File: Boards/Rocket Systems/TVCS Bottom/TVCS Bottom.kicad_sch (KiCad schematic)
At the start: 105 parts, among them J1 Conn_01x01_Socket, J10 Conn_01x01_Socket, J11 Conn_01x01_Socket, J12 Conn_01x01_Socket, J13 Conn_01x01_Socket, J14 Conn_01x01_Socket, J15 Conn_01x01_Socket, J2 Conn_01x01_Socket, J3 XT30UPB-M, J4 XT30UPB-M, J5 Conn_01x01_Socket, J6 XT30UPB-M, J8 Conn_01x01_Socket, J9 Conn_01x01_Socket, Q1 2N7002H6327XTSA2, U1 MAX31856MUD+T, U10 MAX31856MUD+T, U11 IRLZ44NPBF, U12 IRLZ44NPBF, U13 LM61460AASQRJRRQ1, U14 ADS1114IRUGR, U15 TPS1120DR, U16 TPS1120DR, U3 MAX31856MUD+T, U4 MAX485CSA+T, U5 MCP9808T-E/MC, U8 PCA9306DP_118, U9 LM61460AASQRJRRQ1

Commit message: Repo Refactor and new systems update
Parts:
- removed LED6, LED7, LED8, LED9: HSMH-H191, Red SMD LED:HSMHH191, symbol Red SMD LED:HSMH-H191
- removed U15, U16: TPS1120DR, 2 PMOS:D8, symbol Dual PMOS TPS1120DR:TPS1120DR
- removed U4: MAX485CSA+T, RS Transceiver:21-0041-3-M_90-0096-8L_MXM, symbol RS_Transceiver_MAX485:MAX485CSA+T
- removed U8: PCA9306DP_118, I2C Voltage Translator:TSSOP8_SOT505-1_NXP, symbol I2C Voltage Translator:PCA9306DP_118
- added CR2, CR3, CR4, CR5: VLMC3100-GS08, LED_PLCC_VSMB, symbol GreenLED__VLMC3100-GS08:VLMC3100-GS08
- added U15, U8: TPS1120DR, D8, symbol TPS1120DR:TPS1120DR
- added U17: MAX485CSA+T, 21-0041-3-M_90-0096-8L_MXM, symbol RS_Transceiver:MAX485CSA+T
- added U4: PCA9306DP_118, TSSOP8_SOT505-1_NXP, symbol NXP PCA9306DP:PCA9306DP_118
- D1, D3: footprint Schottky RSX301L:DIOM5026X220N -> DIOM5026X220N
- J3, J4, J6: footprint AMASS_XT30UPB-M:CONN_XT30UPB-M_AMA -> CONN_XT30UPB-M_AMA
- Q1: footprint (none) -> PG-SOT23-3-5_INF_MIN
- U1, U10, U3: footprint Thermocouple:21-0066J_14_MXM -> 21-0066J_14_MXM
- U11, U12: footprint NMOS IRLZ44:PG-TO220-3_INF -> PG-TO220-3_INF
- U13, U9: footprint DCDC_LM61460:VQFN-HR14_RJR_TEX -> VQFN-HR14_RJR_TEX
- U14: footprint ADS1114:RUG10 -> RUG10
- U5: footprint MCP9808-TempSensor:DFN8_2x3MC_MCH -> DFN8_2x3MC_MCH
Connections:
- net +3.3V: now also U4.2 (VREF1)
- net +5V: now also U17.8 (VCC)
- net ADC SDA I2C: now also U4.4 (SDA1)
- net ADC SDL I2C: now also U4.3 (SCL1)
- net GND: now also CR2.1, CR3.1, CR4.1, CR5.1, U17.5 (GND), U4.1 (GND)
- net RS_ENABLE: now also U15.4 (2GATE), U17.2 (*RE), U17.3 (DE)
- net RS_RX: now also U17.1 (RO)
- net RS_TX: now also U17.4 (DI)
- net THERMO1_~{CS}: now also U8.2 (1GATE)
- net THERMO2_~{CS}: now also U8.4 (2GATE)
- net THERMO3_~{CS}: now also U15.2 (1GATE)
- net at C23.1, R4.1: now also U4.7 (VREF2), U4.8 (EN)
- net at R18.1: now also U8.1 (1SOURCE)
- net at R19.1: now also U8.3 (2SOURCE)
- net at J2.1 (Pin_1), R15.1, R16.1: now also U17.7 (B)
- net at J5.1 (Pin_1), R11.2, R16.2: now also U17.6 (A)
- net at R34.2, U14.10 (SCL): now also U4.6 (SCL2)
- net at R40.2, U14.9 (SDA): now also U4.5 (SDA2)
- net at R20.1: now also U15.1 (1SOURCE)
- net at R21.1: now also U15.3 (2SOURCE)
- new net: CR3.2, U8.5 (2DRAIN), U8.6 (2DRAIN)
- new net: CR5.2, U15.5 (2DRAIN), U15.6 (2DRAIN)
- new net: CR4.2, U15.7 (1DRAIN), U15.8 (1DRAIN)
- new net: CR2.2, U8.7 (1DRAIN), U8.8 (1DRAIN)
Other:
- sheet RP2040 Standard ports: added GPIO10, GPIO9; removed GP10/SPI1 SCK, GP9/SPI1 ~{CS}
- title: CANha Board -> Temperature & Valve Control System B
- moved on the sheet: R18, R19, R20, R21

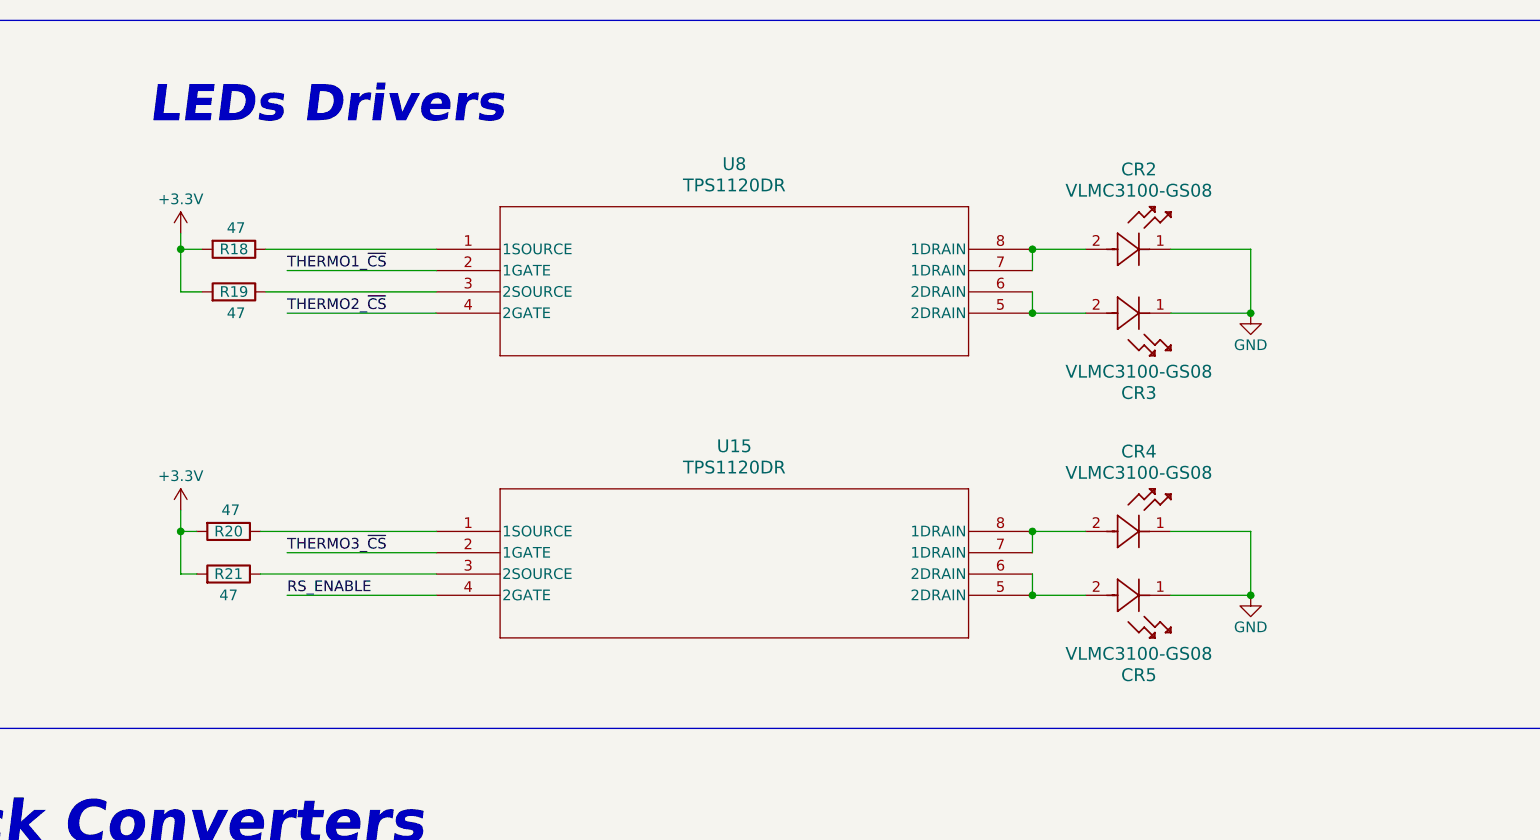
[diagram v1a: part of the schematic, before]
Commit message: Led driver circuit correction & RF FEM implementation
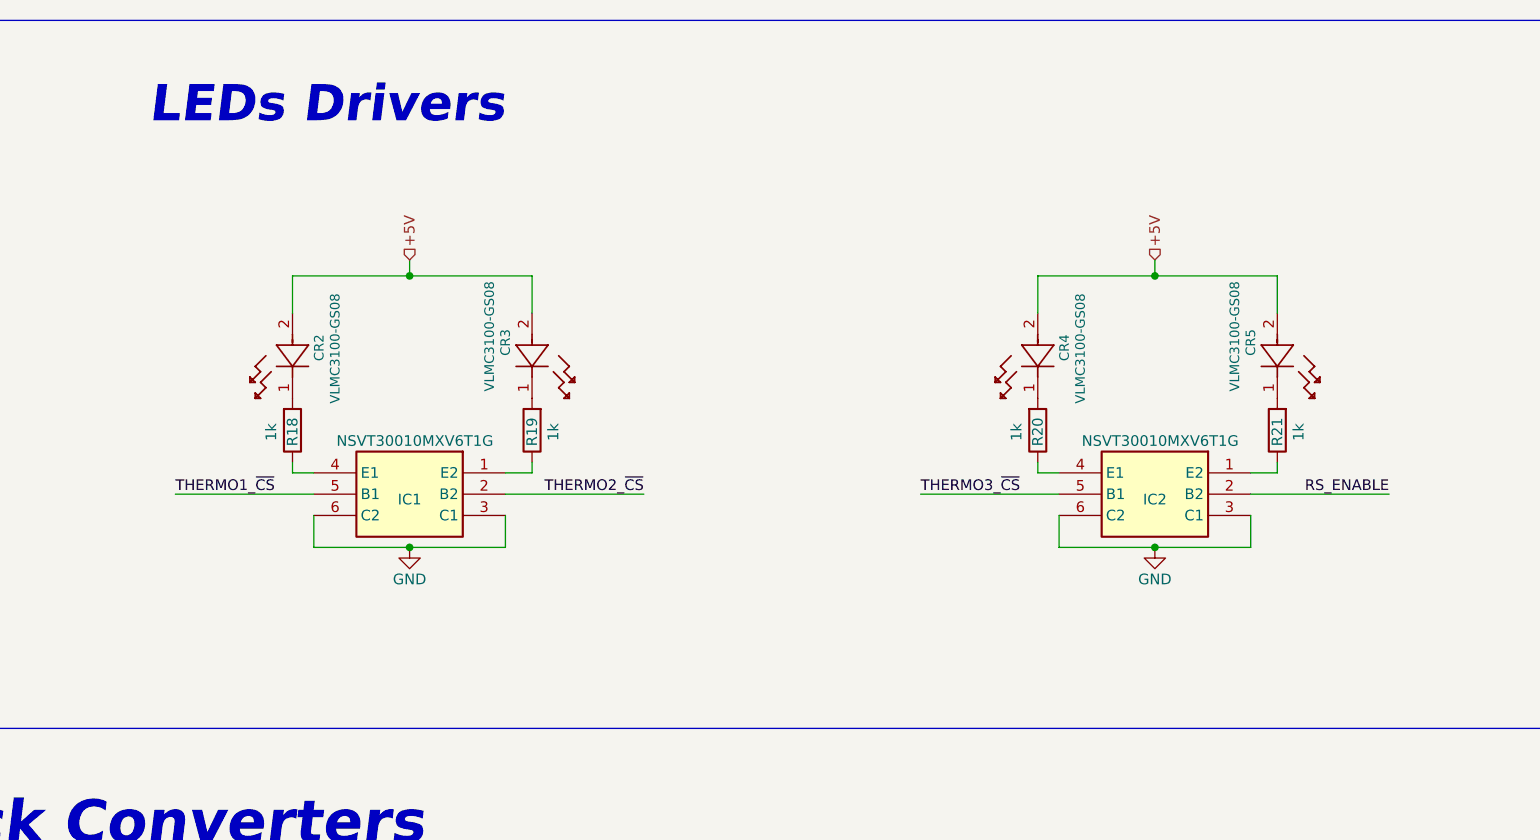
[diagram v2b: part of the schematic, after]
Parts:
- removed U15, U8: TPS1120DR, D8, symbol TPS1120DR:TPS1120DR
- added IC1, IC2: NSVT30010MXV6T1G, SOTFL50P160X60-6N, symbol NSVT30010MXV6T1G:NSVT30010MXV6T1G
- R18, R19, R20, R21: value 47 -> 1k; footprint RES_0402:RES_0402 -> RC0402N_VIS:RC0402N_VIS
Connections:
- net +3.3V: no longer R18.2, R19.2, R20.2, R21.2
- net +5V: now also CR2.2, CR3.2, CR4.2, CR5.2
- net GND: now also IC1.3 (C1), IC1.6 (C2), IC2.3 (C1), IC2.6 (C2); no longer CR2.1, CR3.1, CR4.1, CR5.1
- net RS_ENABLE: now also IC2.2 (B2)
- net THERMO1_~{CS}: now also IC1.5 (B1)
- net THERMO2_~{CS}: now also IC1.2 (B2)
- net THERMO3_~{CS}: now also IC2.5 (B1)
- net at R19.1: now also IC1.1 (E2)
- net at R21.1: now also IC2.1 (E2)
- net at R20.1: now also IC2.4 (E1)
- net at R18.1: now also IC1.4 (E1)
- new net: CR2.1, R18.2
- new net: CR5.1, R21.2
- new net: CR4.1, R20.2
- new net: CR3.1, R19.2

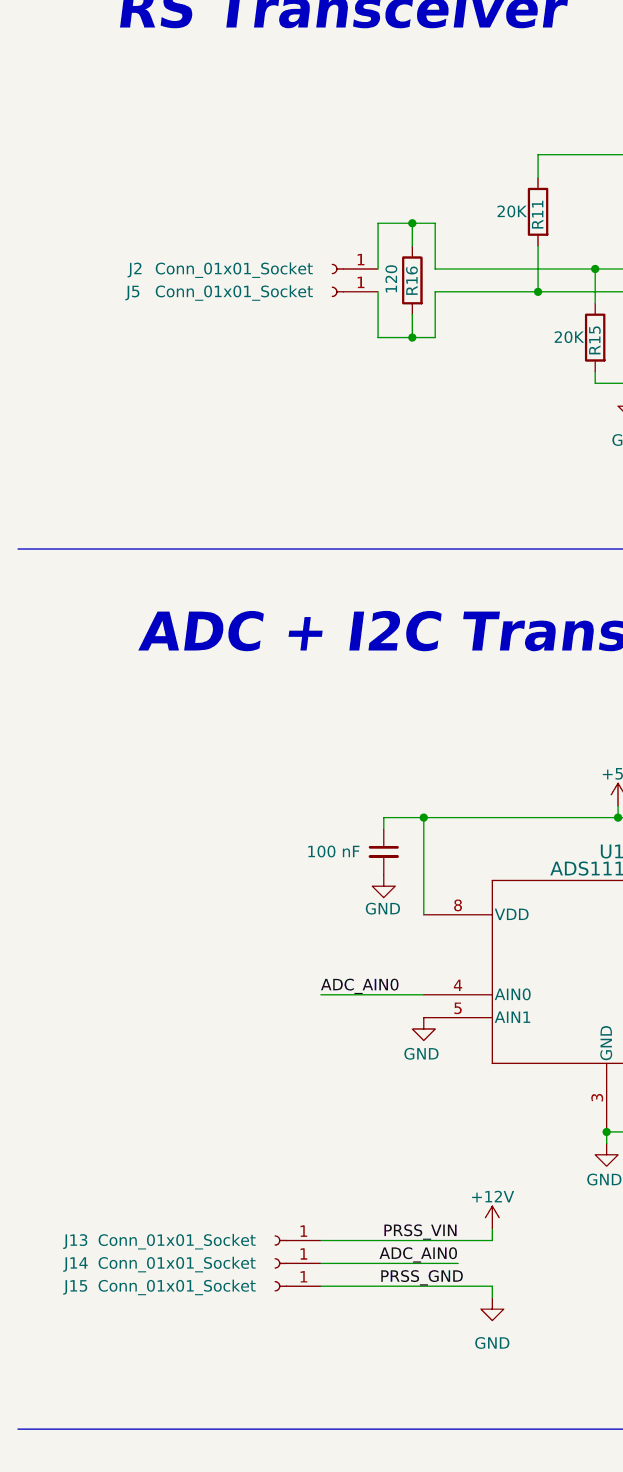
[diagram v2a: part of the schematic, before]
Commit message: Connectors RS e ADC
Connectors nas TVCS e no OBC
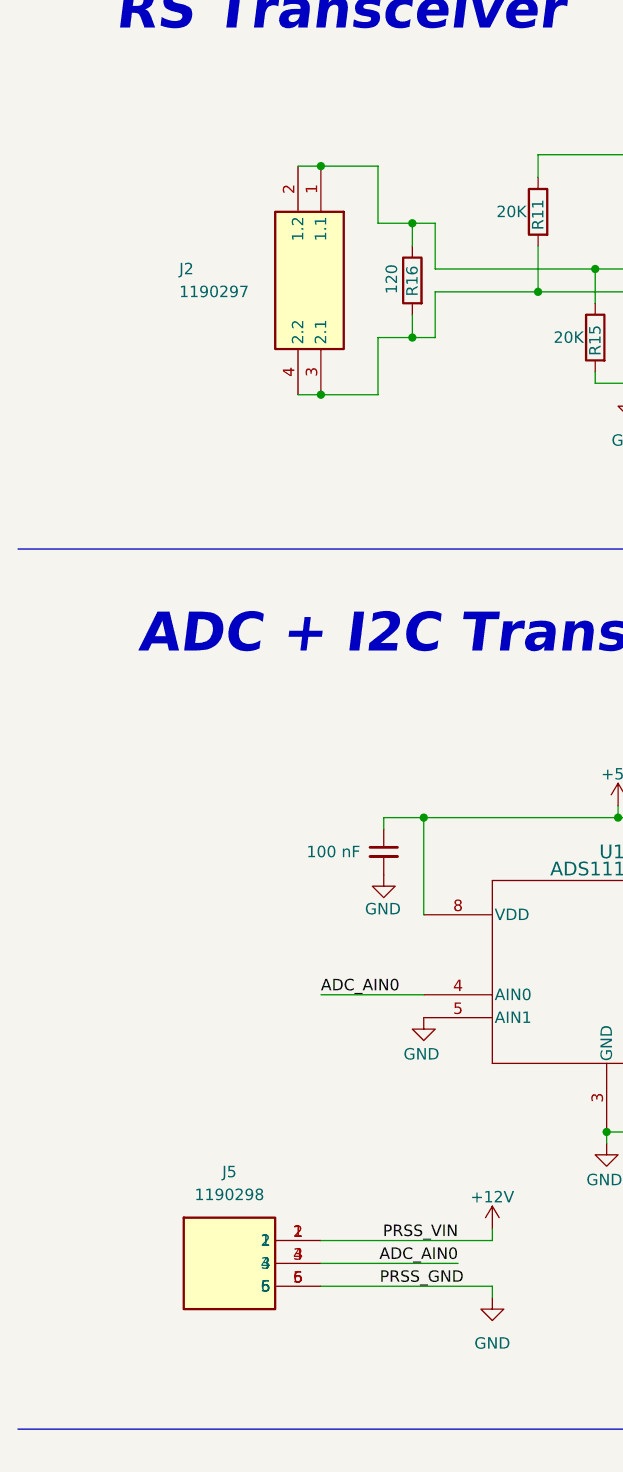
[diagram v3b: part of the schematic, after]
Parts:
- removed J13, J14, J15, J2, J5: Conn_01x01_Socket, Button_Switch_THT:SW_Lever_1P2T_NKK_GW12LxH, symbol Connector:Conn_01x01_Socket
- added J2: 1190297, 1190297, symbol 1190297:1190297
- added J5: 1190298, LPT Conn 3 Entradas:1190298, symbol 1190298:1190298
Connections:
- net +12V: now also J5.1, J5.2
- net ADC_AIN0: now also J5.3, J5.4
- net GND: now also J5.5, J5.6
- net at R15.1, R16.1, U17.7 (B): now also J2.1 (1.1), J2.2 (1.2)
- net at R11.2, R16.2, U17.6 (A): now also J2.3 (2.1), J2.4 (2.2)

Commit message: Mais Sockets Pico
TVCS Top, Bottom and Fill and G&F COMMS
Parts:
- added J13, J14, J15, J17: Conn_01x01_Socket, Pico_Conn1x1:Pico_01pin, symbol Connector:Conn_01x01_Socket
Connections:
- net RP2040 Standard/GP26_ADC0: now also J13.1 (Pin_1)
- net RP2040 Standard/GP27_ADC1: now also J14.1 (Pin_1)
- net RP2040 Standard/GP28_ADC2: now also J15.1 (Pin_1)
- net RP2040 Standard/GP29_ADC3: now also J17.1 (Pin_1)
- no-connect marks 4 -> 0

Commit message: XT30 to XT60
Connectores atualizados em toda as TVCS
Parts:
- removed J3, J4, J6: XT30UPB-M, CONN_XT30UPB-M_AMA, symbol AMASS_XT30UPB-M:XT30UPB-M
- added J3, J4, J6: XT60PW-M, Conn XT60PW-M:AMASS_XT60PW-M, symbol XT60PW-M:XT60PW-M
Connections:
- net +12V: now also J3.2 (-), J4.2 (-)
- net +16V: now also J6.2 (-)
- net GND: now also J6.1 (+)
- net at D1.2 (A), U12.2: now also J4.1 (+)
- net at D3.2 (A), U11.2: now also J3.1 (+)
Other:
- moved on the sheet: C_BT1, C_FF1, C_VCC1, D3, L3, R17, R_ENT1, R_FBB1, R_FBT1, R_FF1, R_PG1, R_RT1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

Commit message: Library
Vários Footprints de Capacitors e Inductors
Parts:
- C1, C10, C11, C17, C18, C19, C2, C20, C23, C3, C4, C6, C7, C8, C9: footprint Capacitor_0402:Capacitor_0402 -> Capacitor-0402:Capacitor_0402
- CR2, CR3, CR4, CR5: footprint LED_PLCC_VSMB -> LED-Green_VLMC3100-GS08:LED_PLCC_VSMB
- D1, D3: footprint DIOM5026X220N -> Diode-Schottky_RSX301L:DIOM5026X220N
- IC1, IC2: footprint SOTFL50P160X60-6N -> 2 PNP:SOTFL50P160X60-6N
- J2: footprint 1190297 -> LPT Conn 2 Entradas:1190297
- Q1: footprint PG-SOT23-3-5_INF_MIN -> NMOS_2N7002:PG-SOT23-3-5_INF_MIN
- U1, U10, U3: footprint 21-0066J_14_MXM -> Thermocouple:21-0066J_14_MXM
- U11, U12: footprint PG-TO220-3_INF -> NMOS IRLZ44:PG-TO220-3_INF
- U13, U9: footprint VQFN-HR14_RJR_TEX -> DCDC_LM61460:VQFN-HR14_RJR_TEX
- U14: footprint RUG10 -> ADS1114:RUG10
- U17: footprint 21-0041-3-M_90-0096-8L_MXM -> RS Transceiver:21-0041-3-M_90-0096-8L_MXM
- U4: footprint TSSOP8_SOT505-1_NXP -> I2C Voltage Translator:TSSOP8_SOT505-1_NXP
- U5: footprint DFN8_2x3MC_MCH -> MCP9808-TempSensor:DFN8_2x3MC_MCH
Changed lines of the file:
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@@
 			)
 		)
-		(property "Footprint" "Capacitor_0402:Capacitor_0402"
+		(property "Footprint" "Capacitor-0402:Capacitor_0402"
 			(at 127.3048 325.755 0)
 			(effects
@@
 			)
 		)
-		(property "Footprint" "Capacitor_0402:Capacitor_0402"
+		(property "Footprint" "Capacitor-0402:Capacitor_0402"
 			(at 48.26 109.22 0)
 			(effects
@@
 			)
 		)
-		(property "Footprint" "TSSOP8_SOT505-1_NXP"
+		(property "Footprint" "I2C Voltage Translator:TSSOP8_SOT505-1_NXP"
 			(at 184.15 309.245 0)
 			(effects
@@
 			)
 		)
-		(property "Footprint" "PG-TO220-3_INF"
+		(property "Footprint" "NMOS IRLZ44:PG-TO220-3_INF"
 			(at 65.278 421.386 0)
 			(effects
@@
 			)
 		)
-		(property "Footprint" "21-0041-3-M_90-0096-8L_MXM"
+		(property "Footprint" "RS Transceiver:21-0041-3-M_90-0096-8L_MXM"
 			(at 121.92 237.49 0)
 			(effects
@@
 			)
 		)
-		(property "Footprint" "Capacitor_0402:Capacitor_0402"
+		(property "Footprint" "Capacitor-0402:Capacitor_0402"
 			(at 59.055 95.25 0)
 			(effects
@@
 			)
 		)
-		(property "Footprint" "Capacitor_0402:Capacitor_0402"
+		(property "Footprint" "Capacitor-0402:Capacitor_0402"
 			(at 52.705 304.8 0)
 			(effects
@@
 			)
 		)
-		(property "Footprint" "PG-SOT23-3-5_INF_MIN"
+		(property "Footprint" "NMOS_2N7002:PG-SOT23-3-5_INF_MIN"
 			(at 139.065 345.44 0)
 			(effects
@@
 			)
 		)
-		(property "Footprint" "Capacitor_0402:Capacitor_0402"
+		(property "Footprint" "Capacitor-0402:Capacitor_0402"
 			(at 52.705 95.25 0)
 			(effects
@@
 			)
 		)
-		(property "Footprint" "Capacitor_0402:Capacitor_0402"
+		(property "Footprint" "Capacitor-0402:Capacitor_0402"
 			(at 46.99 59.055 0)
 			(effects
@@
 			)
 		)
-		(property "Footprint" "LED_PLCC_VSMB"
+		(property "Footprint" "LED-Green_VLMC3100-GS08:LED_PLCC_VSMB"
 			(at 283.845 173.355 0)
 			(effects
@@
 			)
 		)
-		(property "Footprint" "RUG10"
+		(property "Footprint" "ADS1114:RUG10"
 			(at 57.15 323.215 0)
 			(effects
@@
 			)
 		)
-		(property "Footprint" "LED_PLCC_VSMB"
+		(property "Footprint" "LED-Green_VLMC3100-GS08:LED_PLCC_VSMB"
 			(at 401.32 173.355 0)
 			(effects
@@
 			)
 		)
-		(property "Footprint" "1190297"
+		(property "Footprint" "LPT Conn 2 Entradas:1190297"
 			(at -49.2 250.19 0)
 			(effects
@@
 			)
 		)
-		(property "Footprint" "Capacitor_0402:Capacitor_0402"
+		(property "Footprint" "Capacitor-0402:Capacitor_0402"
 			(at 148.59 59.69 0)
 			(effects
@@
 			)
 		)
-		(property "Footprint" "Capacitor_0402:Capacitor_0402"
+		(property "Footprint" "Capacitor-0402:Capacitor_0402"
 			(at 48.26 114.3 0)
 			(effects
@@
 			)
 		)
-		(property "Footprint" "DIOM5026X220N"
+		(property "Footprint" "Diode-Schottky_RSX301L:DIOM5026X220N"
 			(at -27.61 402.59 0)
 			(effects
@@
 			)
 		)
-		(property "Footprint" "SOTFL50P160X60-6N"
+		(property "Footprint" "2 PNP:SOTFL50P160X60-6N"
 			(at 379.095 287.325 0)
 			(effects
@@
 			)
 		)
-		(property "Footprint" "DFN8_2x3MC_MCH"
+		(property "Footprint" "MCP9808-TempSensor:DFN8_2x3MC_MCH"
 			(at 147.955 109.22 0)
 			(effects
@@
 			)
 		)
-		(property "Footprint" "Capacitor_0402:Capacitor_0402"
+		(property "Footprint" "Capacitor-0402:Capacitor_0402"
 			(at 148.59 54.61 0)
 			(effects
@@
 			)
 		)
-		(property "Footprint" "SOTFL50P160X60-6N"
+		(property "Footprint" "2 PNP:SOTFL50P160X60-6N"
 			(at 290.195 287.325 0)
 			(effects
@@
 			)
 		)
-		(property "Footprint" "DIOM5026X220N"
+		(property "Footprint" "Diode-Schottky_RSX301L:DIOM5026X220N"
 			(at 51.13 402.59 0)
 			(effects
@@
 			)
 		)
-		(property "Footprint" "VQFN-HR14_RJR_TEX"
+		(property "Footprint" "DCDC_LM61460:VQFN-HR14_RJR_TEX"
 			(at 302.387 384.175 0)
 			(effects
@@
 			)
 		)
-		(property "Footprint" "21-0066J_14_MXM"
+		(property "Footprint" "Thermocouple:21-0066J_14_MXM"
 			(at 53.975 98.298 0)
 			(effects
@@
 			)
 		)
-		(property "Footprint" "Capacitor_0402:Capacitor_0402"
+		(property "Footprint" "Capacitor-0402:Capacitor_0402"
 			(at 51.435 40.005 0)
 			(effects
@@
 			)
 		)
-		(property "Footprint" "Capacitor_0402:Capacitor_0402"
+		(property "Footprint" "Capacitor-0402:Capacitor_0402"
 			(at 57.785 40.005 0)
 			(effects
@@
 			)
 		)
-		(property "Footprint" "LED_PLCC_VSMB"
+		(property "Footprint" "LED-Green_VLMC3100-GS08:LED_PLCC_VSMB"
 			(at 372.745 173.355 0)
 			(effects
@@
 			)
 		)
-		(property "Footprint" "Capacitor_0402:Capacitor_0402"
+		(property "Footprint" "Capacitor-0402:Capacitor_0402"
 			(at 159.385 40.64 0)
 			(effects
@@
 			)
 		)
-		(property "Footprint" "21-0066J_14_MXM"
+		(property "Footprint" "Thermocouple:21-0066J_14_MXM"
 			(at 154.305 43.688 0)
 			(effects
@@
 			)
 		)
-		(property "Footprint" "PG-TO220-3_INF"
+		(property "Footprint" "NMOS IRLZ44:PG-TO220-3_INF"
 			(at 144.018 420.751 0)
 			(effects
@@
 			)
 		)
-		(property "Footprint" "Capacitor_0402:Capacitor_0402"
+		(property "Footprint" "Capacitor-0402:Capacitor_0402"
 			(at 216.2302 119.38 0)
 			(effects
@@
 			)
 		)
-		(property "Footprint" "21-0066J_14_MXM"
+		(property "Footprint" "Thermocouple:21-0066J_14_MXM"
 			(at 52.705 43.053 0)
 			(effects
@@
 			)
 		)
-		(property "Footprint" "LED_PLCC_VSMB"
+		(property "Footprint" "LED-Green_VLMC3100-GS08:LED_PLCC_VSMB"
 			(at 312.42 173.355 0)
 			(effects
@@
 			)
 		)
-		(property "Footprint" "Capacitor_0402:Capacitor_0402"
+		(property "Footprint" "Capacitor-0402:Capacitor_0402"
 			(at 153.035 40.64 0)
 			(effects
@@
 			)
 		)
-		(property "Footprint" "VQFN-HR14_RJR_TEX"
+		(property "Footprint" "DCDC_LM61460:VQFN-HR14_RJR_TEX"
 			(at 312.547 290.83 0)
 			(effects
@@
 			)
 		)
-		(property "Footprint" "Capacitor_0402:Capacitor_0402"
+		(property "Footprint" "Capacitor-0402:Capacitor_0402"
 			(at 46.99 53.975 0)
 			(effects
